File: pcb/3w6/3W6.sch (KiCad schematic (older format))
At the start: 105 parts, among them J1 USB_C Main, J2 USB_C I2C_L, J3 USB_C I2C_R, SW1 SW_Push, SW10 SW_Push, SW11 SW_Push, SW12 SW_Push, SW13 SW_Push, SW14 SW_Push, SW15 SW_Push, SW16 SW_Push, SW17 Trackball_Choc_Combi, SW18 SW_Push, SW19 SW_Push, SW2 SW_Push, SW20 SW_Push, SW21 SW_Push, SW22 SW_Push, SW23 SW_Push, SW24 SW_Push, SW25 SW_Push, SW26 SW_Push, SW27 SW_Push, SW28 SW_Push, SW29 SW_Push, SW3 SW_Push, SW30 SW_Push, SW31 SW_Push, SW32 SW_Push, SW33 SW_Push, SW34 SW_Push, SW35 SW_Push, SW36 SW_Push, SW37 SW_Push, SW4 SW_Push, SW5 SW_Push, SW6 SW_Push, SW7 SW_Push, SW8 SW_Push, SW9 SW_Push, U1 ATmega32U4-AU, U2 TCA9555RTWR, Y1 16MHZ

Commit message: making files ready for production
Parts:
- removed D38, D53: D, Weteor:D_SOD-123, symbol Device:D_Small
- removed U2: TCA9555RTWR, Package_DFN_QFN:WQFN-24-1EP_4x4mm_P0.5mm_EP2.45x2.45mm, symbol Interface_Expansion:TCA9555RTWR
- added U2: TCA9535PWR, Package_SO:TSSOP-24_4.4x7.8mm_P0.65mm, symbol Interface_Expansion:TCA9535PWR
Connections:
- net Col_R0: now also U2.4 (P00)
- net Col_R1: now also U2.5 (P01)
- net Col_R2: now also U2.6 (P02)
- net Col_R3: now also U2.7 (P03)
- net Col_R4: now also U2.8 (P04)
- net I2C_SCL_R: now also U2.22 (SCL)
- net I2C_SDA_R: now also U2.23 (SDA)
- net Row_R0: now also U2.13 (P10)
- net Row_R1: now also U2.14 (P11)
- net Row_R2: now also U2.15 (P12)
- net Row_R3: now also U2.16 (P13)
- net VDD: now also U2.24 (VCC)
- net VSS: now also U2.12 (GND), U2.2 (A1), U2.21 (A0), U2.3 (A2)
- net at R5.2: now also U2.1 (~INT)
- no-connect marks 51 -> 48
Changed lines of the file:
@@
 Title "3W6"
 Date "2021-03-18"
-Rev "v1"
+Rev "v2"
 Comp ""
-Comment1 ""
-Comment2 ""
+Comment1 "Licensed under CERN-OHL-P v2"
+Comment2 "(c) weteor"
 Comment3 ""
 Comment4 ""
@@
 	0    1    1    0
 $EndComp
-$Comp
-L Interface_Expansion:TCA9555RTWR U2
-U 1 1 613CD702
-P 3650 6200
-F 0 "U2" H 4050 7150 50  0000 C CNN
-F 1 "TCA9555RTWR" V 3650 6200 50  0000 C CNN
-F 2 "Package_DFN_QFN:WQFN-24-1EP_4x4mm_P0.5mm_EP2.45x2.45mm" H 4850 5200 50  0001 C CNN
-F 3 "http://www.ti.com/lit/ds/symlink/tca9555.pdf" H 3150 7100 50  0001 C CNN
-	1    3650 6200
-	1    0    0    -1
-$EndComp
 Wire Wire Line
 	6000 1100 5900 1100
@@
 	5900 2100 6000 2100
 Wire Wire Line
+	4350 5500 4500 5500
+Wire Wire Line
 	4350 5400 4500 5400
 Wire Wire Line
-	4350 5500 4500 5500
+	4350 6300 4500 6300
+Wire Wire Line
+	4350 6400 4500 6400
+Wire Wire Line
+	4350 6500 4500 6500
 Wire Wire Line
 	4350 6600 4500 6600
-Wire Wire Line
-	4350 6000 4500 6000
-Wire Wire Line
-	4350 6300 4500 6300
-Wire Wire Line
-	4350 6400 4500 6400
-Wire Wire Line
-	4350 6500 4500 6500
-Wire Wire Line
-	4350 5900 4500 5900
-Text Label 4500 6000 0    50   ~ 0
+Text Label 4500 5400 0    50   ~ 0
 Col_R0
-Text Label 4500 6600 0    50   ~ 0
+Text Label 4500 5500 0    50   ~ 0
 Col_R1
-Text Label 4500 5500 0    50   ~ 0
+Text Label 4500 5700 0    50   ~ 0
 Col_R3
-Text Label 4500 5400 0    50   ~ 0
+Text Label 4500 5800 0    50   ~ 0
 Col_R4
 Text Label 4500 6300 0    50   ~ 0
@@
 Text Label 4500 6500 0    50   ~ 0
 Row_R2
-Text Label 4500 5900 0    50   ~ 0
+Text Label 4500 6600 0    50   ~ 0
 Row_R3
 Wire Wire Line
@@
 	3650 7450 3650 7300
 Connection ~ 3250 7450
-Wire Wire Line
-	3650 7450 3750 7450
-Wire Wire Line
-	3750 7450 3750 7300
-Connection ~ 3650 7450
 $Comp
 L power:VSS #PWR010
@@
 Text Label 4550 2200 2    50   ~ 0
 D-
-NoConn ~ 4350 5700
-NoConn ~ 4350 5800
 NoConn ~ 4350 6100
-Text Label 4500 6700 0    50   ~ 0
+Text Label 4500 5600 0    50   ~ 0
 Col_R2
 Wire Wire Line
-	4350 6700 4500 6700
-NoConn ~ 4350 5600
+	4350 5600 4500 5600
 NoConn ~ 3200 650
 NoConn ~ 6000 1800
@@
 NoConn ~ 5350 6600
 NoConn ~ 5350 6800
-NoConn ~ 5150 6800
-NoConn ~ 5150 6600
 $Comp
 L Device:D_Small D43
@@
 	0    -1   -1   0
 $EndComp
-$Comp
-L Device:D_Small D38
-U 1 1 6081F6FF
-P 5150 6700
-F 0 "D38" V 5196 6630 50  0000 R CNN
-F 1 "D" V 5105 6630 50  0000 R CNN
-F 2 "Weteor:D_SOD-123" V 5150 6700 50  0001 C CNN
-F 3 "~" V 5150 6700 50  0001 C CNN
-	1    5150 6700
-	0    -1   -1   0
-$EndComp
 NoConn ~ 6650 6900
-NoConn ~ 6650 7100
 NoConn ~ 6650 6600
 NoConn ~ 6650 6800
 NoConn ~ 6450 6800
 NoConn ~ 6450 6600
-$Comp
-L Device:D_Small D53
-U 1 1 605F2244
-P 6650 7000
-F 0 "D53" V 6696 6930 50  0000 R CNN
-F 1 "D" V 6605 6930 50  0000 R CNN
-F 2 "Weteor:D_SOD-123" V 6650 7000 50  0001 C CNN
-F 3 "~" V 6650 7000 50  0001 C CNN
-	1    6650 7000
-	0    -1   -1   0
-$EndComp
 $Comp
 L Device:D_Small D52
@@
 	0    -1   -1   0
 $EndComp
+$Comp
+L Interface_Expansion:TCA9535PWR U2
+U 1 1 61343A0E
+P 3650 6200
+F 0 "U2" H 3650 7481 50  0000 C CNN
+F 1 "TCA9535PWR" H 3650 7390 50  0000 C CNN
+F 2 "Package_SO:TSSOP-24_4.4x7.8mm_P0.65mm" H 4700 5200 50  0001 C CNN
+F 3 "http://www.ti.com/lit/ds/symlink/tca9535.pdf" H 3150 7100 50  0001 C CNN
+	1    3650 6200
+	1    0    0    -1
+$EndComp
+Wire Wire Line
+	4350 5700 4500 5700
+Wire Wire Line
+	4500 5800 4350 5800
+NoConn ~ 4350 5900
+NoConn ~ 4350 6000
+NoConn ~ 4350 6700
 $EndSCHEMATC

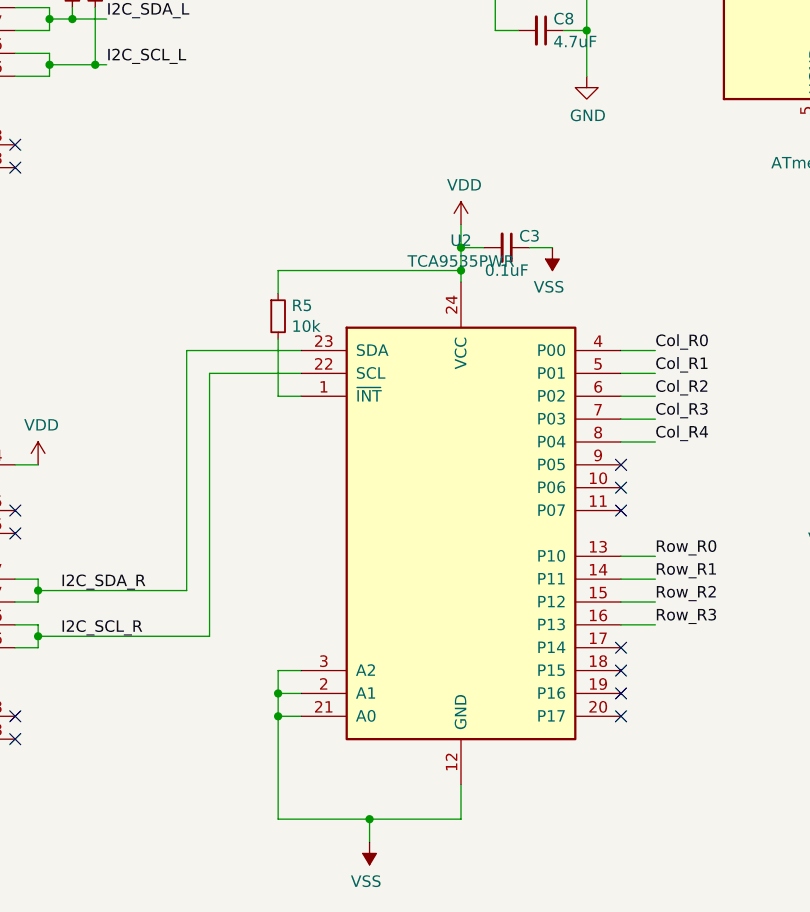
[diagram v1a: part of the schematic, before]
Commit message: fix problems from last production run
changed IO-Expander to PCA9555
moved some vias to connect the copper island around the pimoroni GND pin to board GND
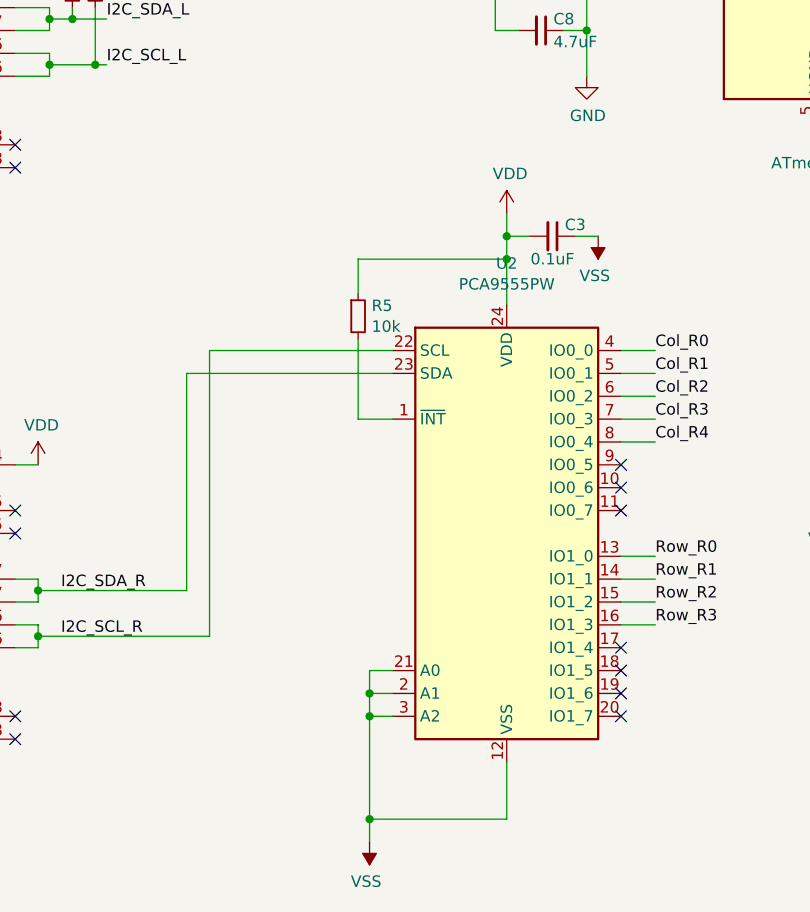
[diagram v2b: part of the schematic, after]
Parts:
- removed U2: TCA9535PWR, Package_SO:TSSOP-24_4.4x7.8mm_P0.65mm, symbol Interface_Expansion:TCA9535PWR
- added U2: PCA9555PW, Package_SO:TSSOP-24_4.4x7.8mm_P0.65mm, symbol Interface_Expansion:PCA9555PW
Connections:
- net Col_R0: now also U2.4 (IO0_0)
- net Col_R1: now also U2.5 (IO0_1)
- net Col_R2: now also U2.6 (IO0_2)
- net Col_R3: now also U2.7 (IO0_3)
- net Col_R4: now also U2.8 (IO0_4)
- net I2C_SCL_R: now also U2.22 (SCL)
- net I2C_SDA_R: now also U2.23 (SDA)
- net Row_R0: now also U2.13 (IO1_0)
- net Row_R1: now also U2.14 (IO1_1)
- net Row_R2: now also U2.15 (IO1_2)
- net Row_R3: now also U2.16 (IO1_3)
- net VDD: now also U2.24 (VDD)
- net VSS: now also U2.12 (VSS), U2.2 (A1), U2.21 (A0), U2.3 (A2)
- net at R5.2: now also U2.1 (~INT)
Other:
- moved on the sheet: C3, R5
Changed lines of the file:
@@
 Row_R3
 Wire Wire Line
-	2450 6450 2450 5400
-Wire Wire Line
-	2450 5400 2950 5400
+	2450 6450 2450 5500
 Wire Wire Line
 	1800 6450 2450 6450
 Wire Wire Line
-	2950 5500 2550 5500
-Wire Wire Line
-	2550 5500 2550 6650
-Wire Wire Line
 	1800 6650 2550 6650
 Wire Wire Line
-	2950 6800 2850 6800
-Wire Wire Line
-	2850 6800 2850 6900
-Wire Wire Line
-	2850 7450 3250 7450
-Wire Wire Line
 	3250 7450 3250 7550
-Wire Wire Line
-	2950 6900 2850 6900
-Connection ~ 2850 6900
-Wire Wire Line
-	2850 6900 2850 7000
-Wire Wire Line
-	2950 7000 2850 7000
-Connection ~ 2850 7000
-Wire Wire Line
-	2850 7000 2850 7450
-Wire Wire Line
-	3250 7450 3650 7450
-Wire Wire Line
-	3650 7450 3650 7300
 Connection ~ 3250 7450
 $Comp
@@
 F 3 "" H 3250 7550 50  0001 C CNN
 	1    3250 7550
-	-1   0    0    1
-$EndComp
-Wire Wire Line
-	3650 5100 3650 5050
-$Comp
-L Device:C_Small C3
-U 1 1 6194E0AE
-P 3850 4950
-F 0 "C3" V 3800 5050 50  0000 C CNN
-F 1 "0.1uF" V 3950 4950 50  0000 C CNN
-F 2 "Weteor:C_0402_HandSolder" H 3850 4950 50  0001 C CNN
-F 3 "~" H 3850 4950 50  0001 C CNN
-	1    3850 4950
-	0    1    1    0
-$EndComp
-$Comp
-L Device:R_Small R5
-U 1 1 619500F8
-P 2850 5250
-F 0 "R5" H 2909 5296 50  0000 L CNN
-F 1 "10k" H 2909 5205 50  0000 L CNN
-F 2 "Weteor:R_0402_HandSolder" H 2850 5250 50  0001 C CNN
-F 3 "~" H 2850 5250 50  0001 C CNN
-	1    2850 5250
-	1    0    0    -1
-$EndComp
-Wire Wire Line
-	2850 5350 2850 5600
-Wire Wire Line
-	2850 5600 2950 5600
-Wire Wire Line
-	2850 5150 2850 5050
-Wire Wire Line
-	2850 5050 3650 5050
-Connection ~ 3650 5050
-Wire Wire Line
-	3750 4950 3650 4950
-Wire Wire Line
-	3650 4950 3650 5050
-Wire Wire Line
-	3950 4950 4050 4950
-$Comp
-L power:VSS #PWR015
-U 1 1 61A0BBD0
-P 4050 4950
-F 0 "#PWR015" H 4050 4800 50  0001 C CNN
-F 1 "VSS" H 4065 5123 50  0000 C CNN
-F 2 "" H 4050 4950 50  0001 C CNN
-F 3 "" H 4050 4950 50  0001 C CNN
-	1    4050 4950
 	-1   0    0    1
 $EndComp
@@
 NoConn ~ 6000 2000
 NoConn ~ 6000 2100
-Connection ~ 3650 4950
-Wire Wire Line
-	3650 4850 3650 4950
-$Comp
-L power:VDD #PWR012
-U 1 1 618443C9
-P 3650 4850
-F 0 "#PWR012" H 3650 4700 50  0001 C CNN
-F 1 "VDD" H 3665 5023 50  0000 C CNN
-F 2 "" H 3650 4850 50  0001 C CNN
-F 3 "" H 3650 4850 50  0001 C CNN
-	1    3650 4850
-	1    0    0    -1
-$EndComp
 $Comp
 L power:VDD #PWR0101
@@
 	0    -1   -1   0
 $EndComp
-$Comp
-L Interface_Expansion:TCA9535PWR U2
-U 1 1 61343A0E
-P 3650 6200
-F 0 "U2" H 3650 7481 50  0000 C CNN
-F 1 "TCA9535PWR" H 3650 7390 50  0000 C CNN
-F 2 "Package_SO:TSSOP-24_4.4x7.8mm_P0.65mm" H 4700 5200 50  0001 C CNN
-F 3 "http://www.ti.com/lit/ds/symlink/tca9535.pdf" H 3150 7100 50  0001 C CNN
-	1    3650 6200
-	1    0    0    -1
-$EndComp
 Wire Wire Line
 	4350 5700 4500 5700
@@
 NoConn ~ 4350 6000
 NoConn ~ 4350 6700
+Wire Wire Line
+	3350 6800 3250 6800
+Wire Wire Line
+	3250 6800 3250 6900
+Wire Wire Line
+	3350 6900 3250 6900
+Connection ~ 3250 6900
+Wire Wire Line
+	3250 6900 3250 7000
+Wire Wire Line
+	3350 7000 3250 7000
+Connection ~ 3250 7000
+Wire Wire Line
+	3250 7000 3250 7450
+Wire Wire Line
+	3250 7450 3850 7450
+Wire Wire Line
+	3850 7200 3850 7450
+$Comp
+L Device:R_Small R5
+U 1 1 619500F8
+P 3200 5250
+F 0 "R5" H 3259 5296 50  0000 L CNN
+F 1 "10k" H 3259 5205 50  0000 L CNN
+F 2 "Weteor:R_0402_HandSolder" H 3200 5250 50  0001 C CNN
+F 3 "~" H 3200 5250 50  0001 C CNN
+	1    3200 5250
+	1    0    0    -1
+$EndComp
+Wire Wire Line
+	3200 5350 3200 5700
+Wire Wire Line
+	3200 5700 3350 5700
+$Comp
+L Device:C_Small C3
+U 1 1 6194E0AE
+P 4050 4900
+F 0 "C3" V 4000 5000 50  0000 C CNN
+F 1 "0.1uF" V 4150 4900 50  0000 C CNN
+F 2 "Weteor:C_0402_HandSolder" H 4050 4900 50  0001 C CNN
+F 3 "~" H 4050 4900 50  0001 C CNN
+	1    4050 4900
+	0    1    1    0
+$EndComp
+Connection ~ 3850 5000
+Wire Wire Line
+	3950 4900 3850 4900
+Wire Wire Line
+	3850 4900 3850 5000
+Wire Wire Line
+	4150 4900 4250 4900
+$Comp
+L power:VSS #PWR015
+U 1 1 61A0BBD0
+P 4250 4900
+F 0 "#PWR015" H 4250 4750 50  0001 C CNN
+F 1 "VSS" H 4265 5073 50  0000 C CNN
+F 2 "" H 4250 4900 50  0001 C CNN
+F 3 "" H 4250 4900 50  0001 C CNN
+	1    4250 4900
+	-1   0    0    1
+$EndComp
+Connection ~ 3850 4900
+Wire Wire Line
+	3850 4800 3850 4900
+$Comp
+L power:VDD #PWR012
+U 1 1 618443C9
+P 3850 4800
+F 0 "#PWR012" H 3850 4650 50  0001 C CNN
+F 1 "VDD" H 3865 4973 50  0000 C CNN
+F 2 "" H 3850 4800 50  0001 C CNN
+F 3 "" H 3850 4800 50  0001 C CNN
+	1    3850 4800
+	1    0    0    -1
+$EndComp
+Wire Wire Line
+	3200 5000 3200 5150
+Wire Wire Line
+	3200 5000 3850 5000
+Wire Wire Line
+	3850 5000 3850 5200
+$Comp
+L Interface_Expansion:PCA9555PW U2
+U 1 1 61038AE6
+P 3850 6200
+F 0 "U2" H 3850 7381 50  0000 C CNN
+F 1 "PCA9555PW" H 3850 7290 50  0000 C CNN
+F 2 "Package_SO:TSSOP-24_4.4x7.8mm_P0.65mm" H 3850 6200 50  0001 C CNN
+F 3 "https://www.nxp.com/docs/en/data-sheet/PCA9555.pdf" H 3850 6200 50  0001 C CNN
+	1    3850 6200
+	1    0    0    -1
+$EndComp
+Wire Wire Line
+	3350 5400 2550 5400
+Wire Wire Line
+	2550 5400 2550 6650
+Wire Wire Line
+	3350 5500 2450 5500
 $EndSCHEMATC
